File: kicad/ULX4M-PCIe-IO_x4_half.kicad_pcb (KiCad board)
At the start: 4 copper layers, 167.7 x 111.2 mm, 255 parts, among them J1 PCIexpress_bracket, J10 FCR684205R, J11 OLED, J12 641737-1, J13 39-30-0060, J14 LM7805_EN, J15 POE, J16 Barrel_Jack, J17 JTAG, J18 I2C_to_ID, J19 PCIe_JTAG, J2 PCIexpress_x4, J20 PCIe_I2C, J21 PCIe_1X_4X, J3 SFP+, J4 SFP+, J5 HAT, J6 EXT_USB, J7 Micro_SD_Card_CD, J8 Board_To_Board, J9 FCR684205T, P1 GPDI0, SW1 SW_DIP_x08, SW2 SW_DIP_x08, U1 TPD4E02B04DQA, U10 TPD4E02B04DQA, U11 TPD4E02B04DQA, U12 TPD4E02B04DQA, U13 AT24CS32-SSHM, U14 LM78M05_TO252, U2 TPD4E02B04DQA, U3 TPD4E02B04DQA, U4 TPD4E02B04DQA, U5 TPD4E02B04DQA, U6 TPD4E02B04DQA, U7 TPD4E02B04DQA, U8 TPD4E02B04DQA, U9 TPD4E02B04DQA

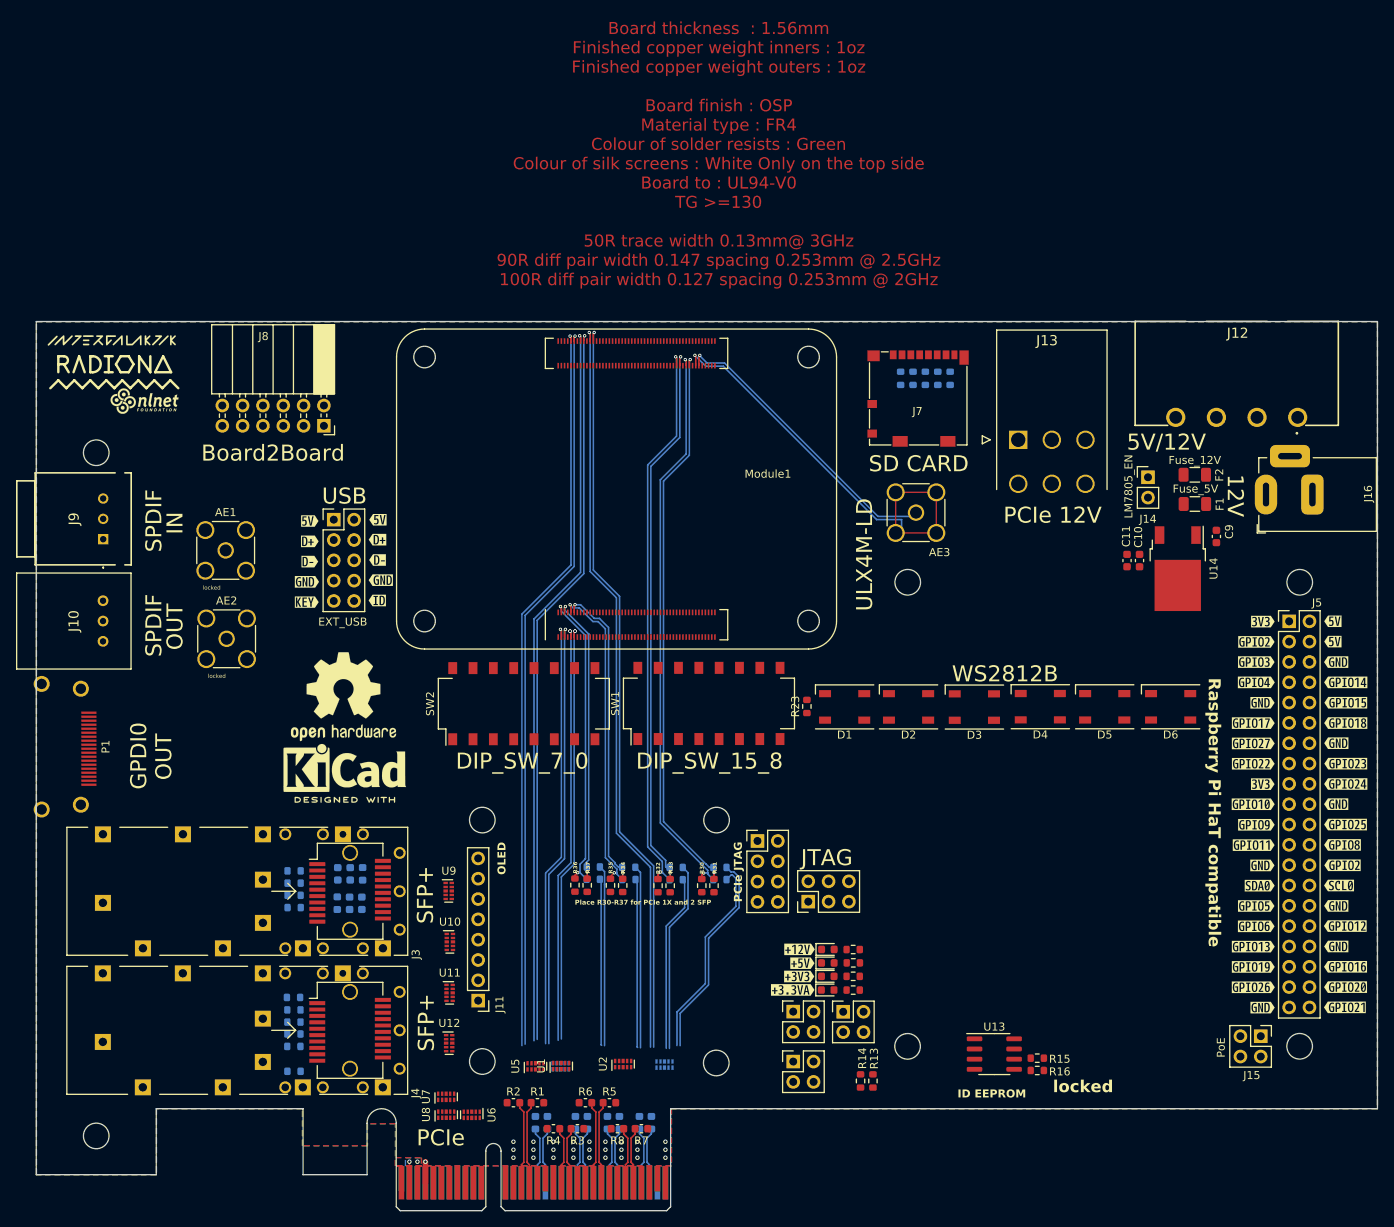
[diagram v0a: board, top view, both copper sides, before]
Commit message: Routing GPIOs
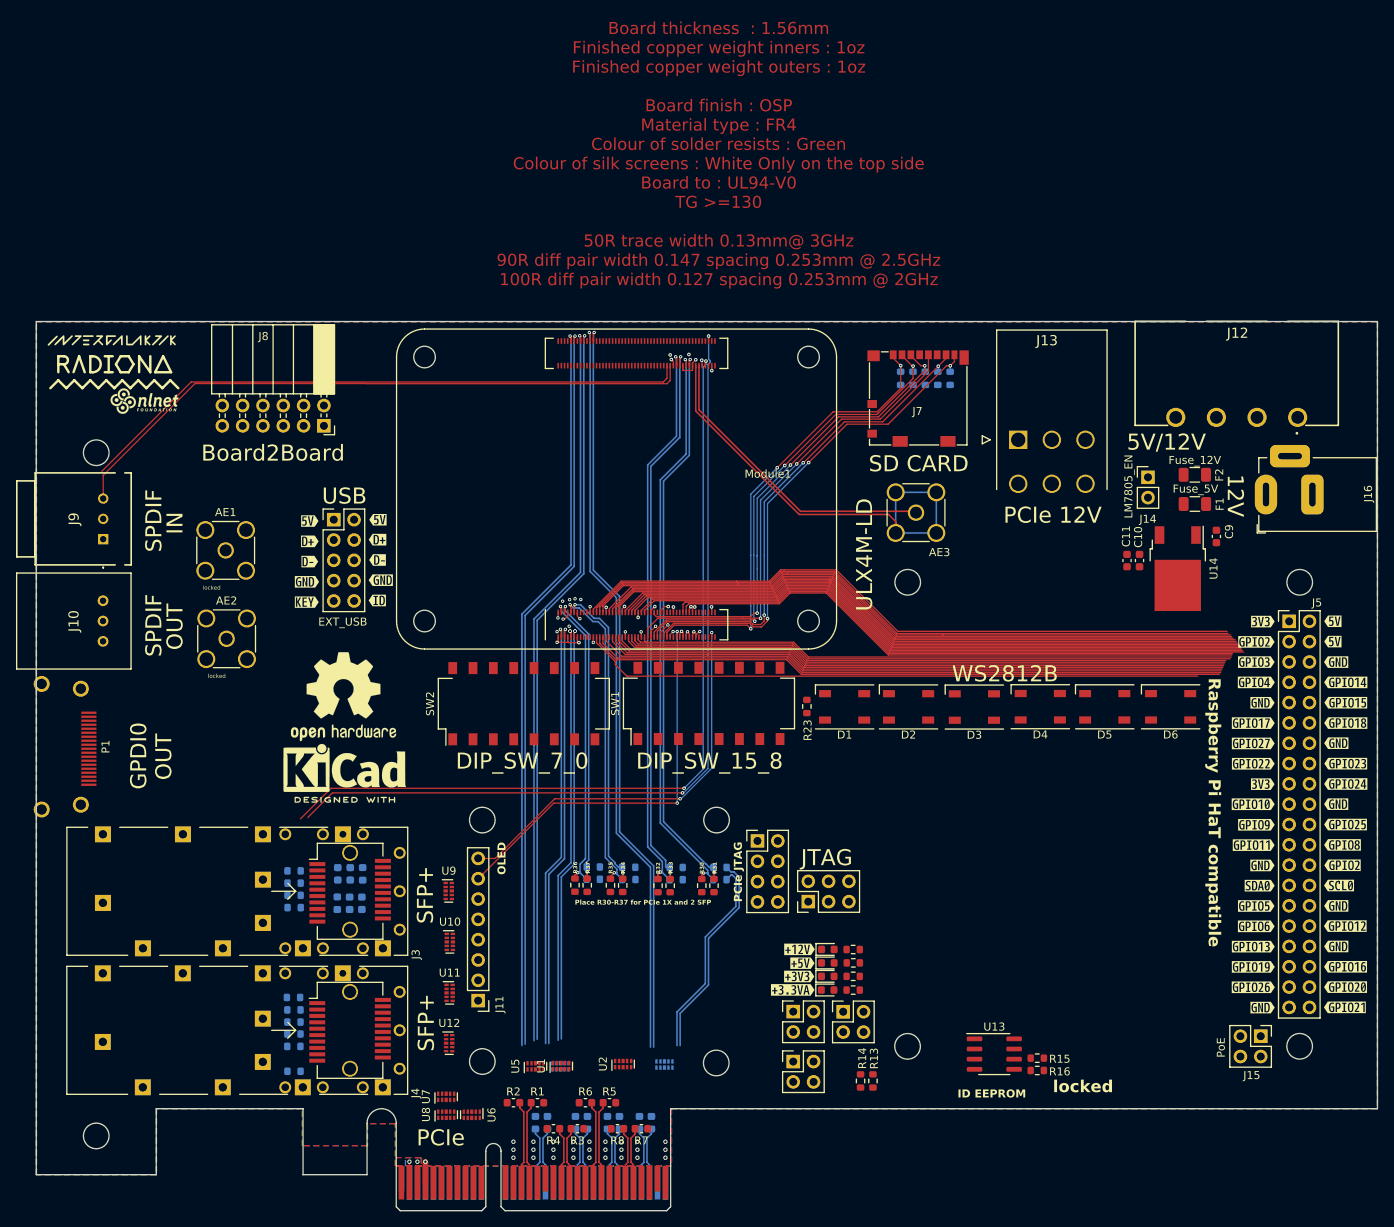
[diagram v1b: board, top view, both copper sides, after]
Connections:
- Module1 pad 169: /CM4_module/DSI0_C_N -> SPDIF_OUT
- Module1 pad 195: SPDIF_OUT -> /CM4_module/DSI1_D2_P
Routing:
- net SFP1_MOD_ABS: track 0.00 -> 107.4 mm, vias 0 -> 2
- net SFP0_MOD_ABS: track 0.00 -> 104.7 mm, vias 0 -> 2
- net GPIO26: track 0.00 -> 84.9 mm
- net GPIO19: track 0.00 -> 84.6 mm
- net GPIO13: track 0.00 -> 84.5 mm
- net GPIO6: track 0.00 -> 84.2 mm
- net GPIO5: track 0.00 -> 83.3 mm
- net ID_SD: track 0.00 -> 83.1 mm
- net GPIO11: track 0.00 -> 82.8 mm
- net GPIO9: track 0.00 -> 82.5 mm
- net GPIO10: track 0.00 -> 81.5 mm
- net GPIO22: track 0.00 -> 81.3 mm
- net GPIO27: track 0.00 -> 80.9 mm
- net SPDIF_IN: track 0.00 -> 80.6 mm
- net GPIO17: track 0.00 -> 80.5 mm
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
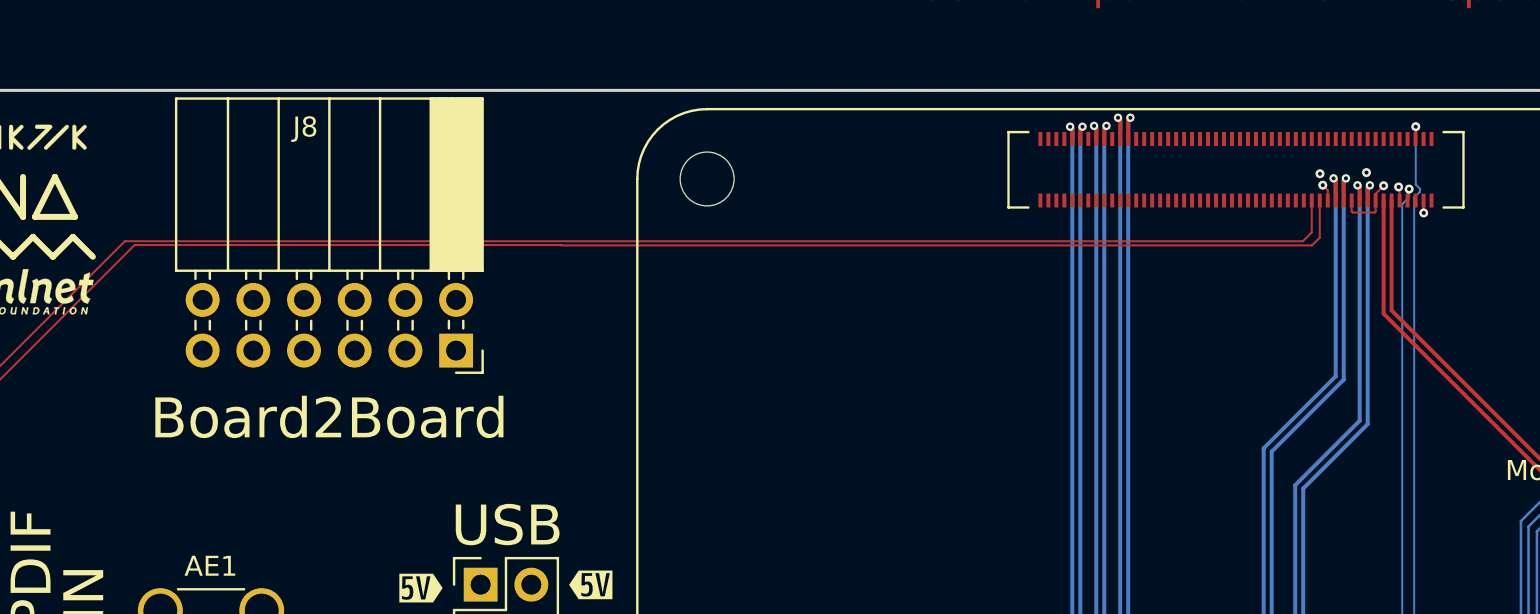
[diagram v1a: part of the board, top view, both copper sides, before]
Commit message: Routing B2B
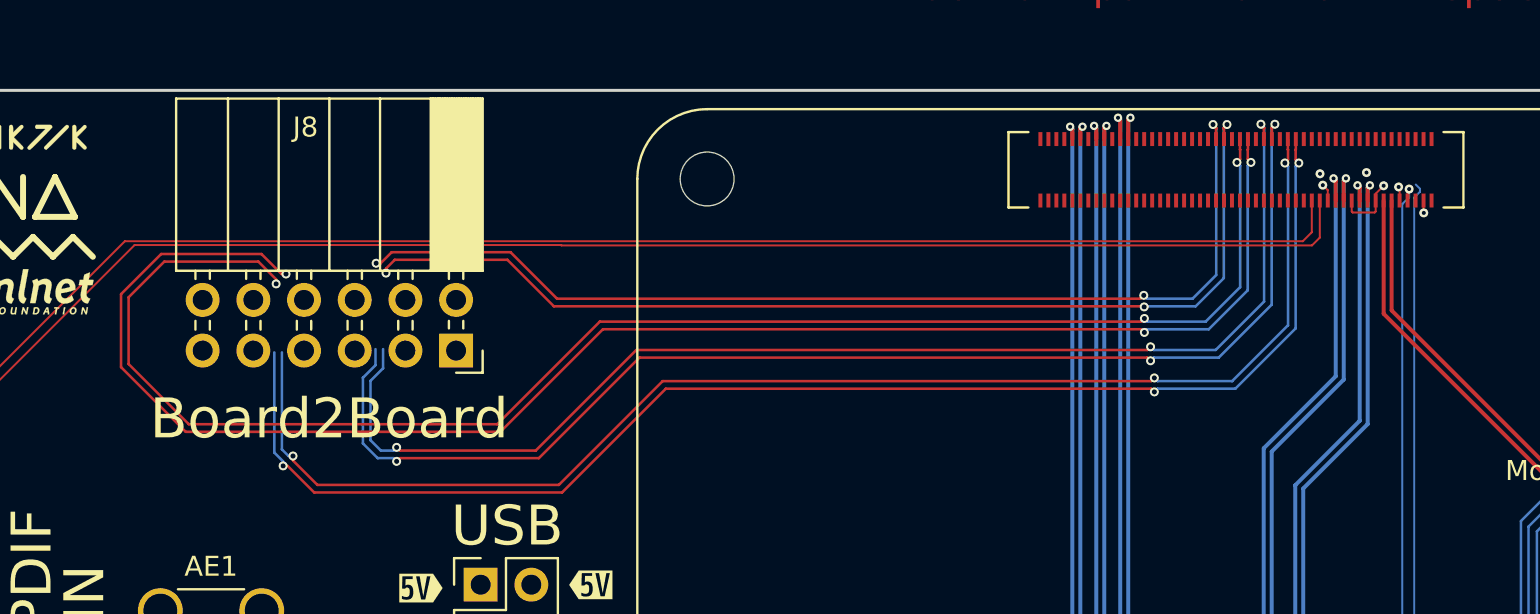
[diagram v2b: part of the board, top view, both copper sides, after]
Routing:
- net GPDI1_TX1_N: track 0.00 -> 81.8 mm, vias 0 -> 3
- net GPDI1_TX1_P: track 0.00 -> 79.6 mm, vias 0 -> 3
- net GPDI1_CLK_N: track 0.00 -> 70.3 mm, vias 0 -> 3
- net GPDI1_CLK_P: track 0.00 -> 69.1 mm, vias 0 -> 3
- net GPDI1_TX0_N: track 0.00 -> 64.2 mm, vias 0 -> 3
- net GPDI1_TX0_P: track 0.00 -> 62.9 mm, vias 0 -> 3
- net GPDI1_TX2_N: track 0.00 -> 52.5 mm, vias 0 -> 3
- net GPDI1_TX2_P: track 0.00 -> 52.3 mm, vias 0 -> 3
- net SFP1_MOD_ABS: track 107.4 -> 103.9 mm, vias 2 -> 1

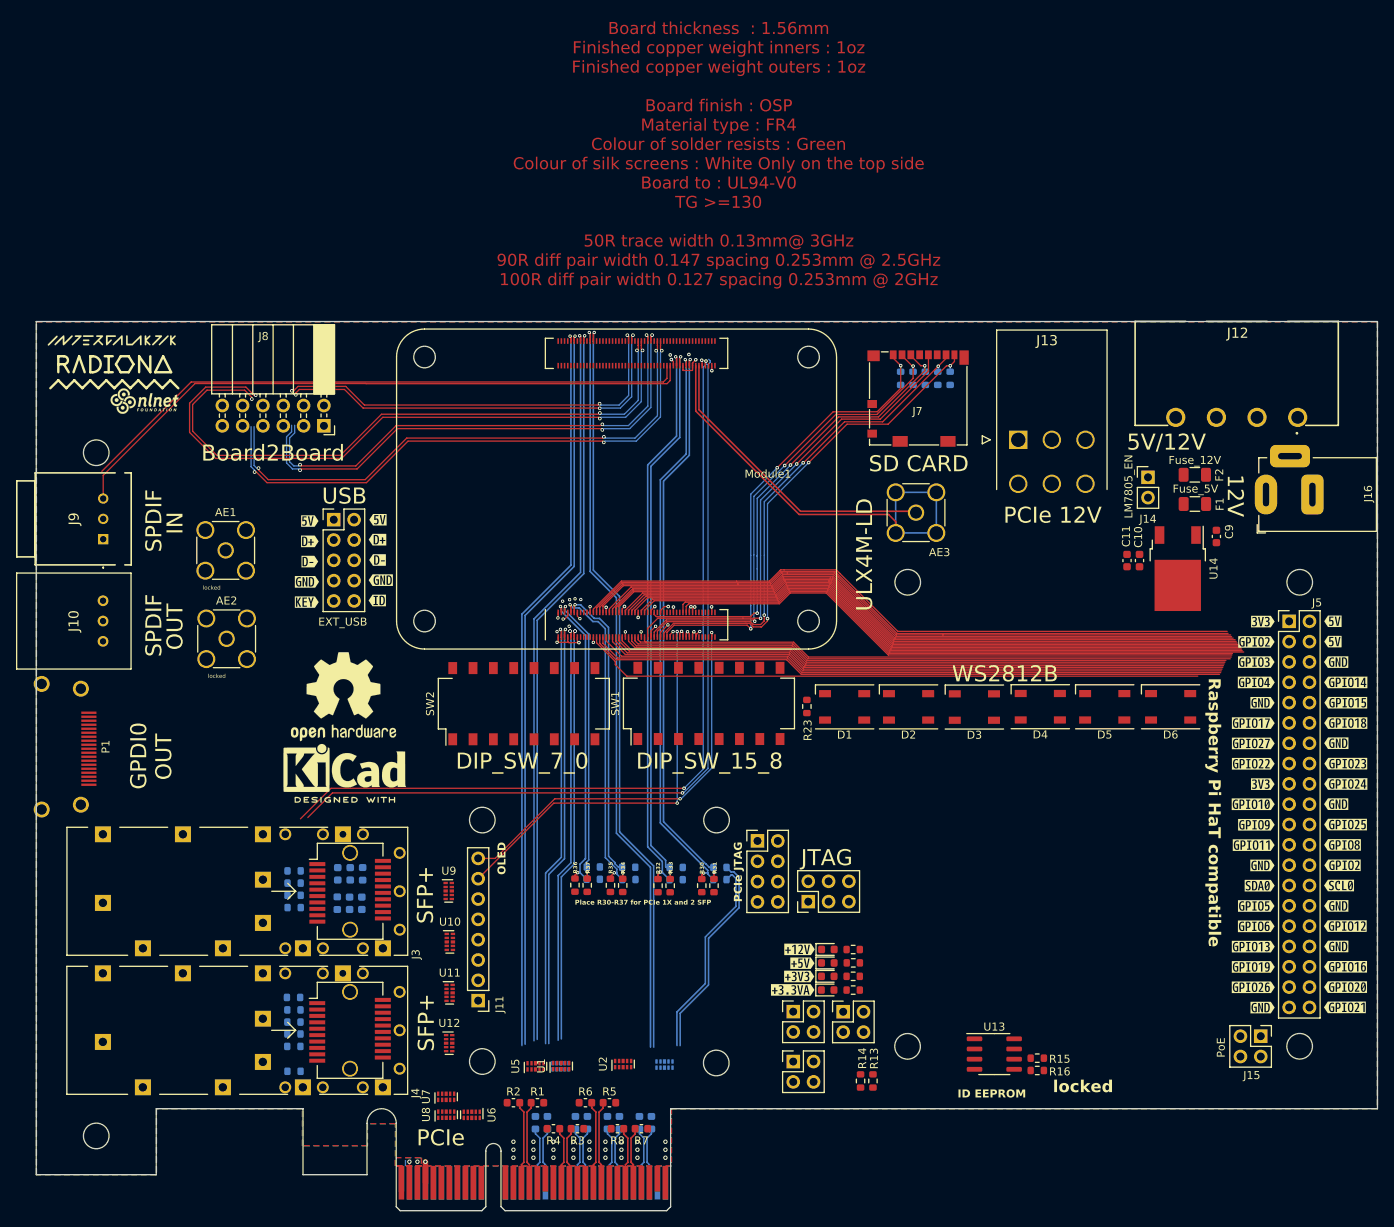
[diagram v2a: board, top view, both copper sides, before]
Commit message: Routing all pins from CM4 connector
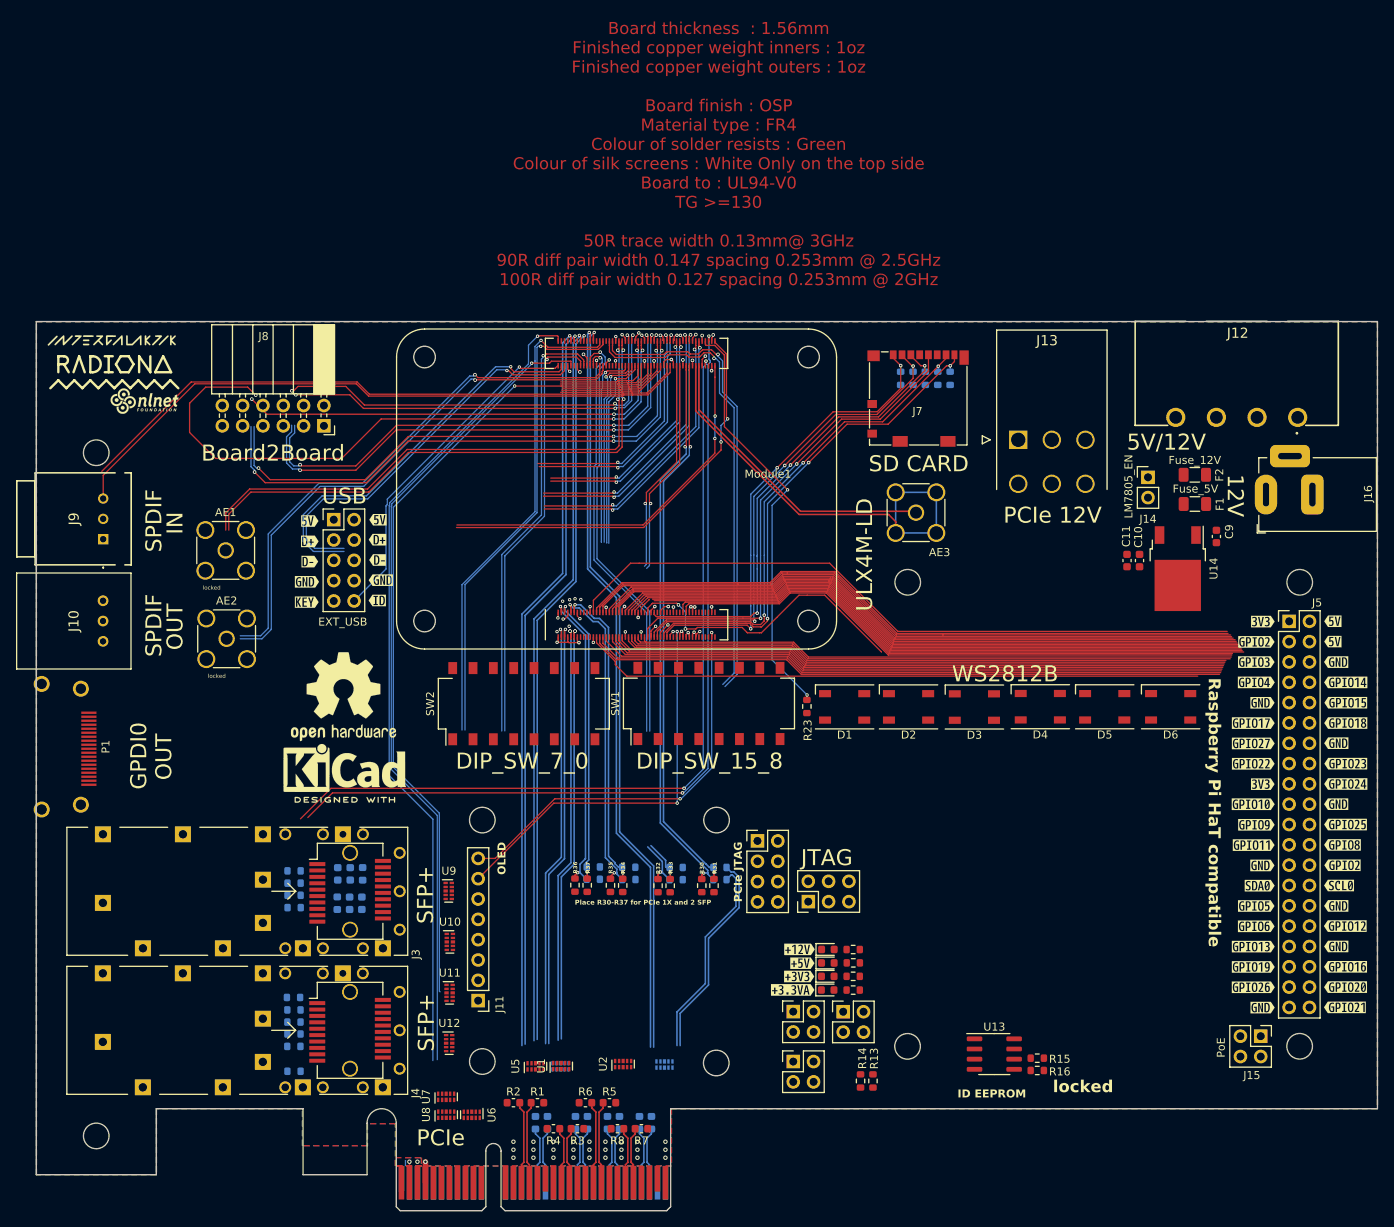
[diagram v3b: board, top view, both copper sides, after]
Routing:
- net /~{WAKE}: track 0.00 -> 103.7 mm, vias 0 -> 1
- net /TX_FAULT_1: track 0.00 -> 102.7 mm, vias 0 -> 1
- net /~{PERST}: track 0.00 -> 102.3 mm, vias 0 -> 1
- net /EXT_CLK_REF1_N: track 0.00 -> 68.2 mm, vias 0 -> 2
- net /EXT_CLK_REF1_P: track 0.00 -> 68.2 mm, vias 0 -> 2
- net /EXT_CLK_REF2_P: track 0.00 -> 67.0 mm, vias 0 -> 1
- net /EXT_CLK_REF2_N: track 0.00 -> 66.7 mm, vias 0 -> 1
- net /CAM0_D0_N: track 0.00 -> 61.1 mm, vias 0 -> 1
- net /CAM0_D0_P: track 0.00 -> 60.7 mm, vias 0 -> 1
- net /CAM0_D1_P: track 0.00 -> 58.4 mm, vias 0 -> 1
- net /CAM0_D1_N: track 0.00 -> 58.1 mm, vias 0 -> 1
- net /CAM1_D0_P: track 0.00 -> 55.2 mm, vias 0 -> 1
- net /CAM1_D0_N: track 0.00 -> 54.0 mm, vias 0 -> 1
- net /CAM1_D1_N: track 0.00 -> 53.4 mm, vias 0 -> 1
- net /RGB_DATA: track 0.00 -> 52.4 mm, vias 0 -> 2
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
